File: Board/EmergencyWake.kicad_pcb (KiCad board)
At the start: 2 copper layers, 100 x 67 mm, 146 parts, among them J1 USB_C_Receptacle_USB2.0, J10 Conn_01x04, J2 Micro_SD_Card_Det, J3 Conn_01x03, J4 Conn_01x02, J5 Conn_01x05, J6 Conn_01x04, J7 Conn_01x02, J8 Conn_01x04, J9 Conn_01x04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

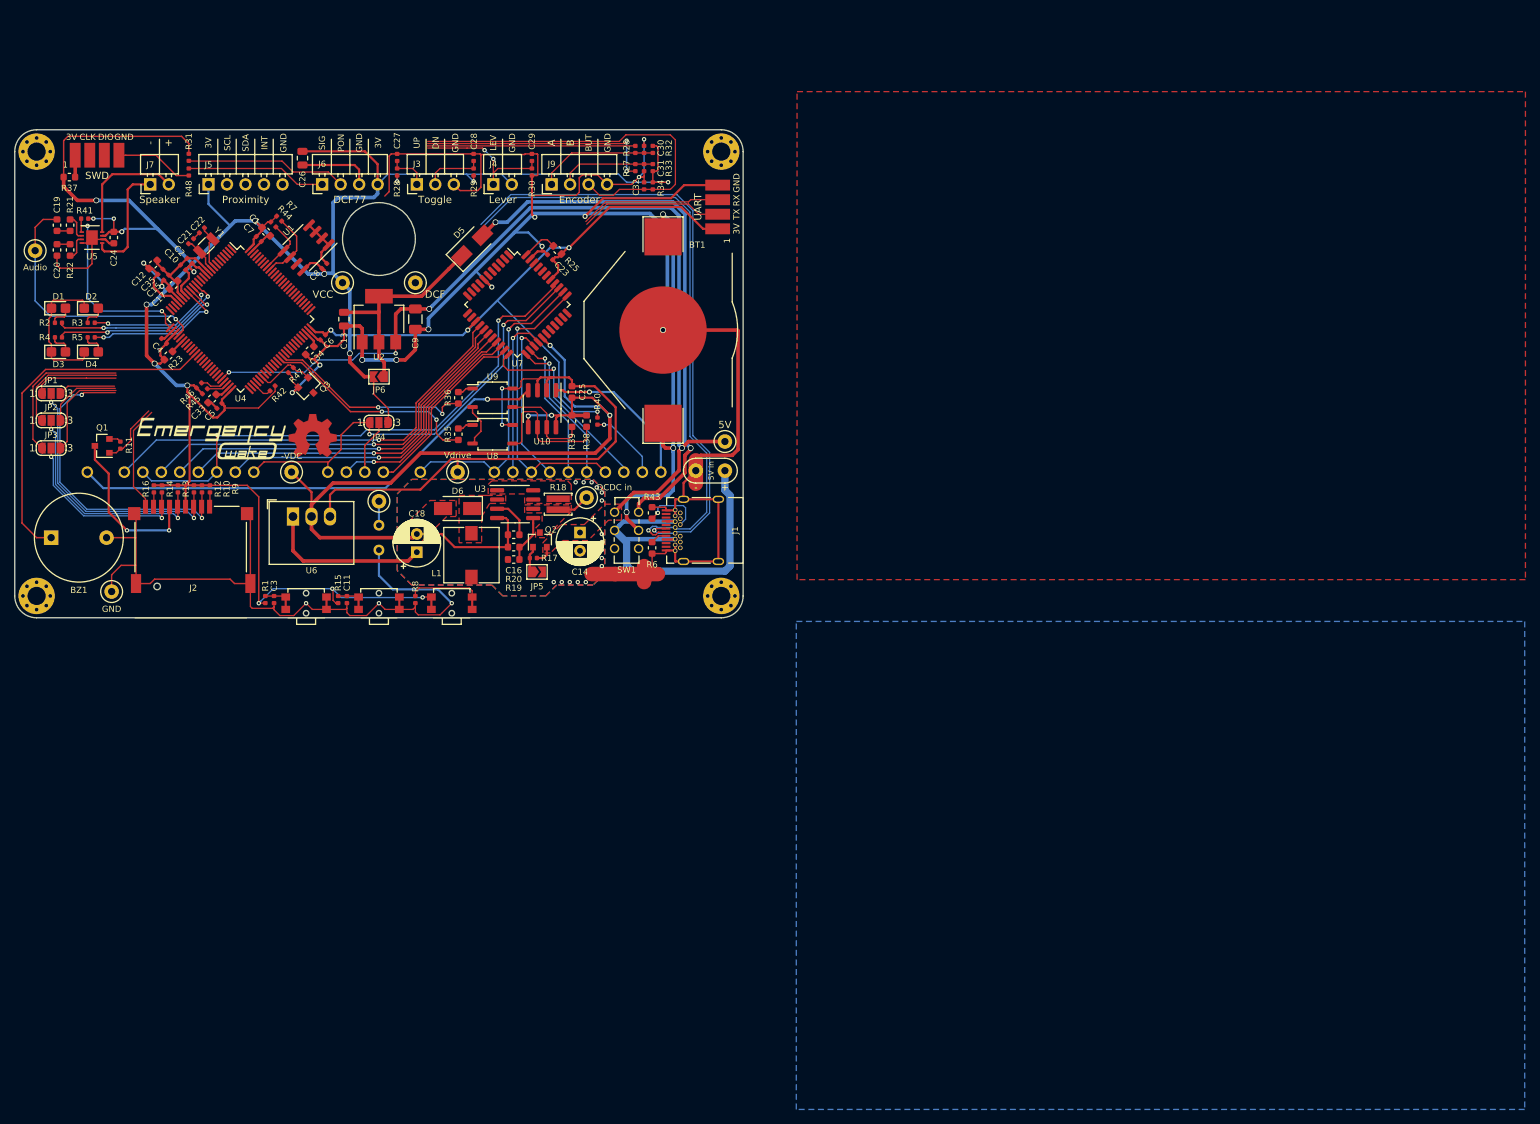
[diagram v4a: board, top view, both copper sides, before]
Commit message: [Board] More routing
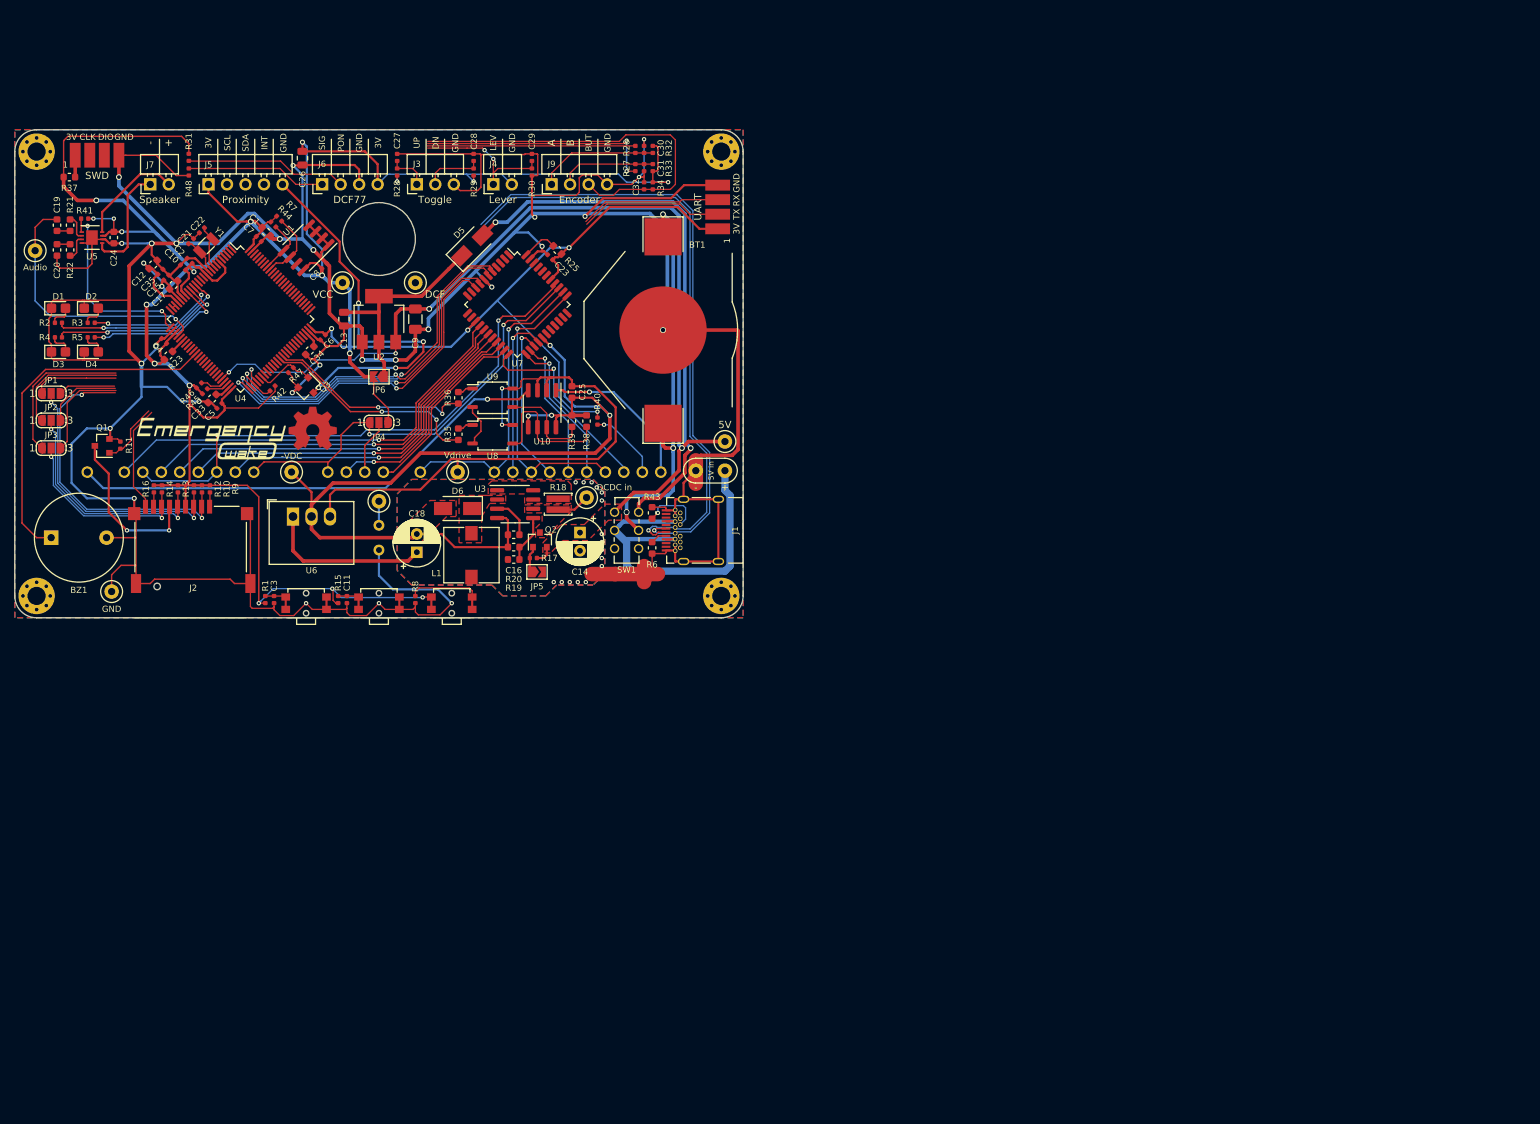
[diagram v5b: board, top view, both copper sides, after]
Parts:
- moved REF** 1.00 mm to (140.9, 141.0)
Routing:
- net GND: track 476.7 -> 629.2 mm, vias 15 -> 27
- net Net-(J5-Pad5): track 0.00 -> 53.1 mm, vias 0 -> 4
- net /VFD_DOUT: track 2.83 -> 52.5 mm, vias 0 -> 2
- net /VFD_DIN: track 0.00 -> 49.6 mm, vias 0 -> 2
- net /VFD_STB: track 0.00 -> 47.5 mm, vias 0 -> 2
- net /VFD_CLK: track 0.00 -> 47.5 mm, vias 0 -> 2
- net VCC: track 469.1 -> 480.1 mm, vias 23 -> 24
- net /SP-: track 16.8 -> 14.6 mm
- net +5V: track 131.6 -> 132.5 mm
- net /LEVER: track 19.7 -> 20.2 mm

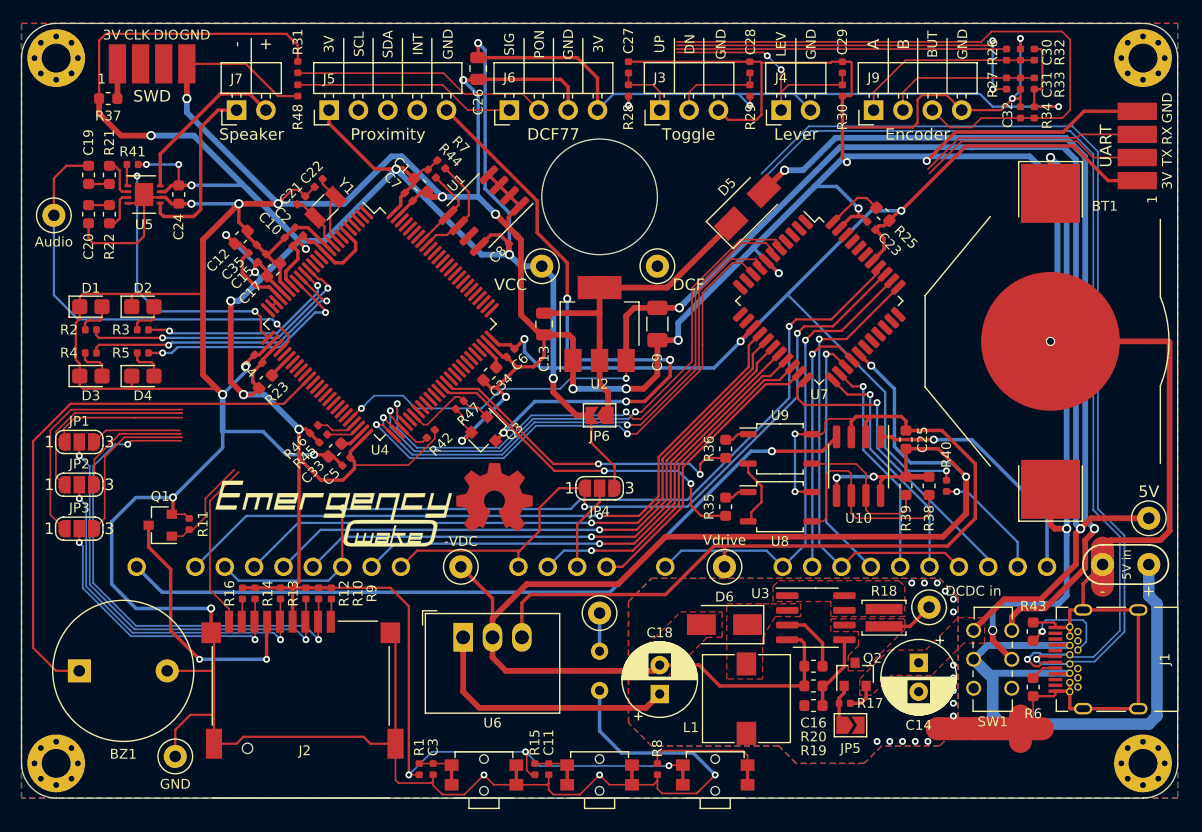
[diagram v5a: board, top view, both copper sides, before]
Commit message: [Board] Routed USB, UART and buttons
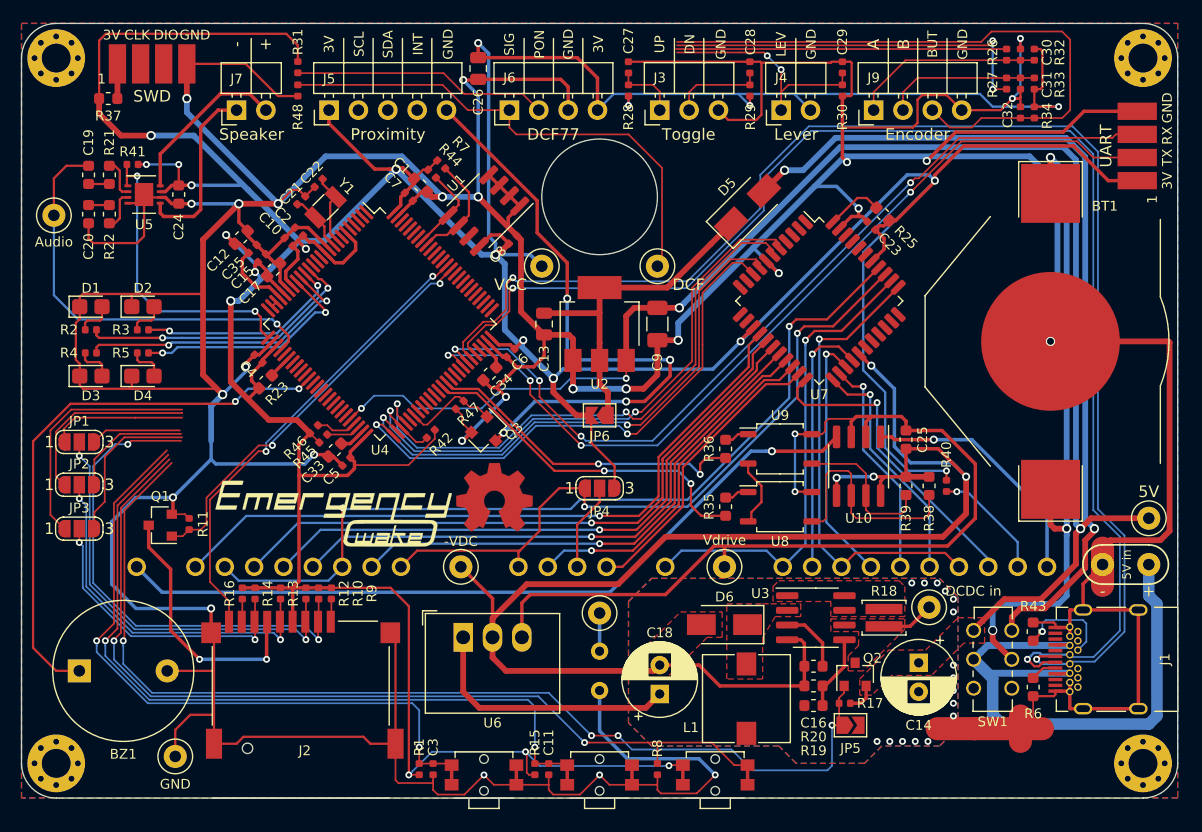
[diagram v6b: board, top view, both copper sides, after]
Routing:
- net /DCDC_EN: track 3.69 -> 92.5 mm, vias 0 -> 4
- net /BOOT0: track 11.3 -> 81.4 mm, vias 0 -> 2
- net /USR_BUT: track 4.56 -> 68.1 mm, vias 0 -> 2
- net /UART_TX: track 19.7 -> 76.8 mm, vias 0 -> 4
- net /UART_RX: track 19.3 -> 75.6 mm, vias 0 -> 4
- net /RESET: track 4.56 -> 59.1 mm, vias 0 -> 2
- net /USB_DM: track 84.8 -> 121.6 mm, vias 1 -> 2
- net /USB_DP: track 85.3 -> 120.7 mm, vias 1 -> 2
- net /SD_EN: track 8.72 -> 35.4 mm, vias 0 -> 2
- net /SD_DET: track 14.7 -> 40.6 mm, vias 0 -> 2
- net /DCF_SIG: track 19.2 -> 44.0 mm
- net VCC: track 480.1 -> 493.1 mm, vias 24 -> 22
- net /BUZZER: vias 0 -> 2

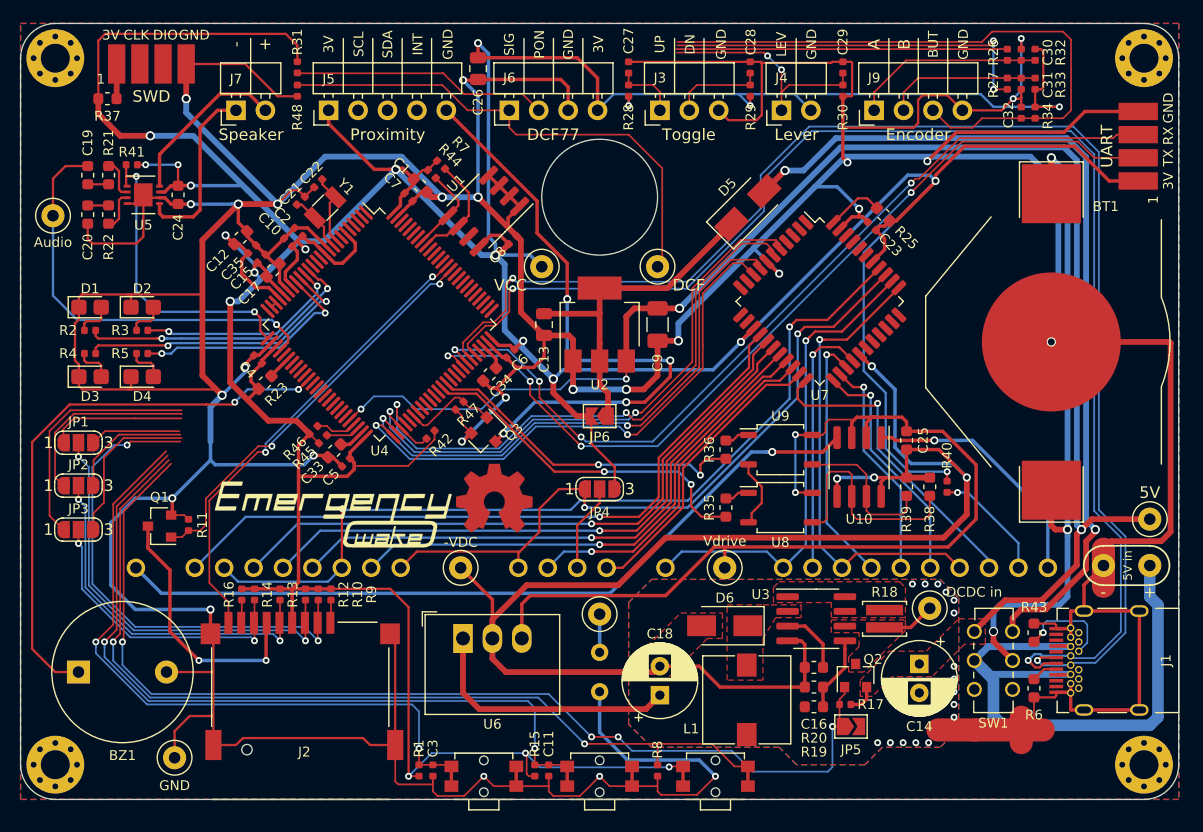
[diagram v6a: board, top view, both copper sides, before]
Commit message: [Board] Added TVS diodes for USB
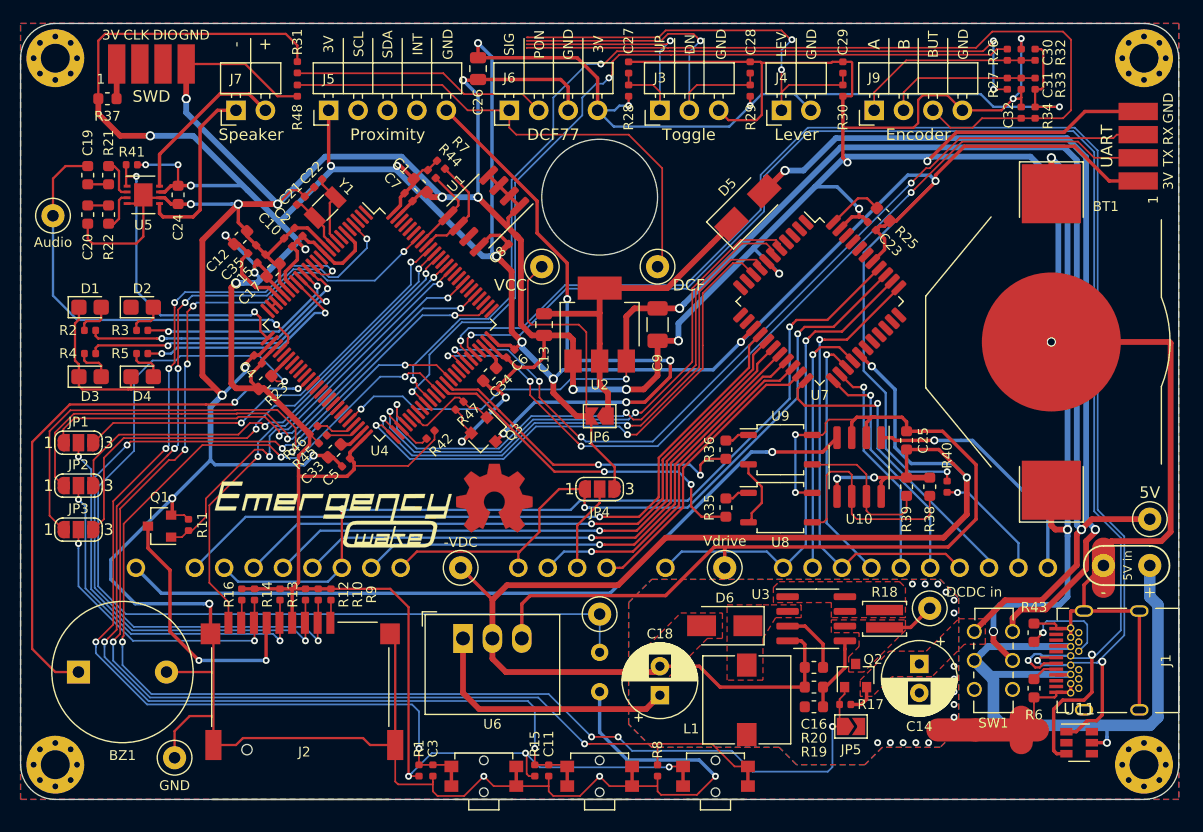
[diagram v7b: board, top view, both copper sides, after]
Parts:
- added U11: SRV05-4, Package_TO_SOT_SMD:SOT-23-6, F.Cu at (191.4, 162.1)
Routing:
- net Net-(R23-Pad2): track 5.39 -> 84.9 mm, vias 0 -> 1
- net /ENC_B: track 32.9 -> 78.6 mm, vias 2 -> 4
- net /ENC_A: track 28.6 -> 73.7 mm, vias 0 -> 2
- net /BOOT0: track 81.4 -> 118.3 mm, vias 2 -> 6
- net /USR_BUT: track 68.1 -> 102.6 mm, vias 2 -> 6
- net /SD_CK: track 16.5 -> 48.2 mm, vias 0 -> 2
- net /SD_CS: track 43.8 -> 74.9 mm, vias 2 -> 4
- net /SD_CMD: track 11.8 -> 42.6 mm, vias 0 -> 2
- net /RESET: track 59.1 -> 89.5 mm, vias 2 -> 6
- net /SD_D0: track 21.1 -> 51.1 mm, vias 0 -> 2
- net /SD_SCK: track 10.6 -> 40.0 mm, vias 0 -> 2
- net /SD_MISO: track 14.0 -> 43.3 mm, vias 0 -> 2
- net /SD_MOSI: track 7.81 -> 37.1 mm, vias 0 -> 2
- net /DCDC_EN: track 92.5 -> 119.7 mm, vias 4 -> 6
- net /TOGGLE_DOWN: track 8.10 -> 30.0 mm, vias 0 -> 1
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
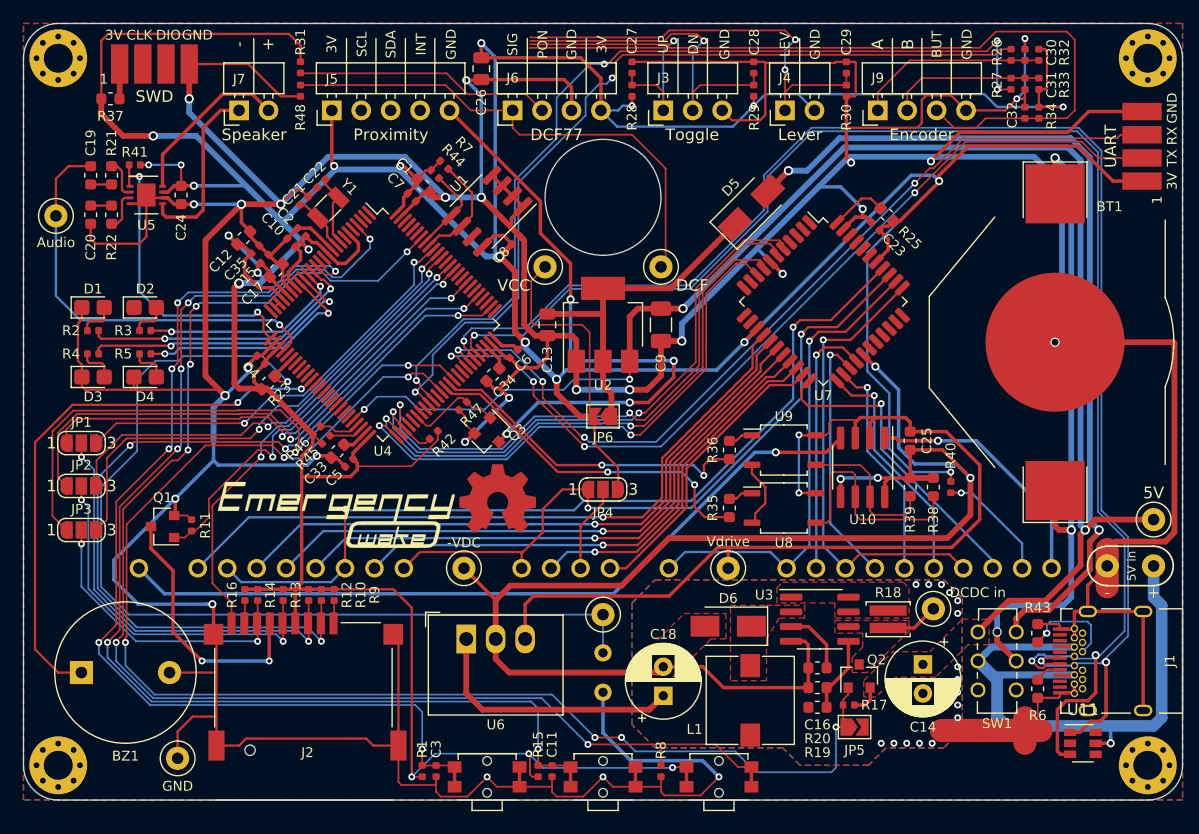
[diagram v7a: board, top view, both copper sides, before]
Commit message: [Board] Routing done, cleanup necessary
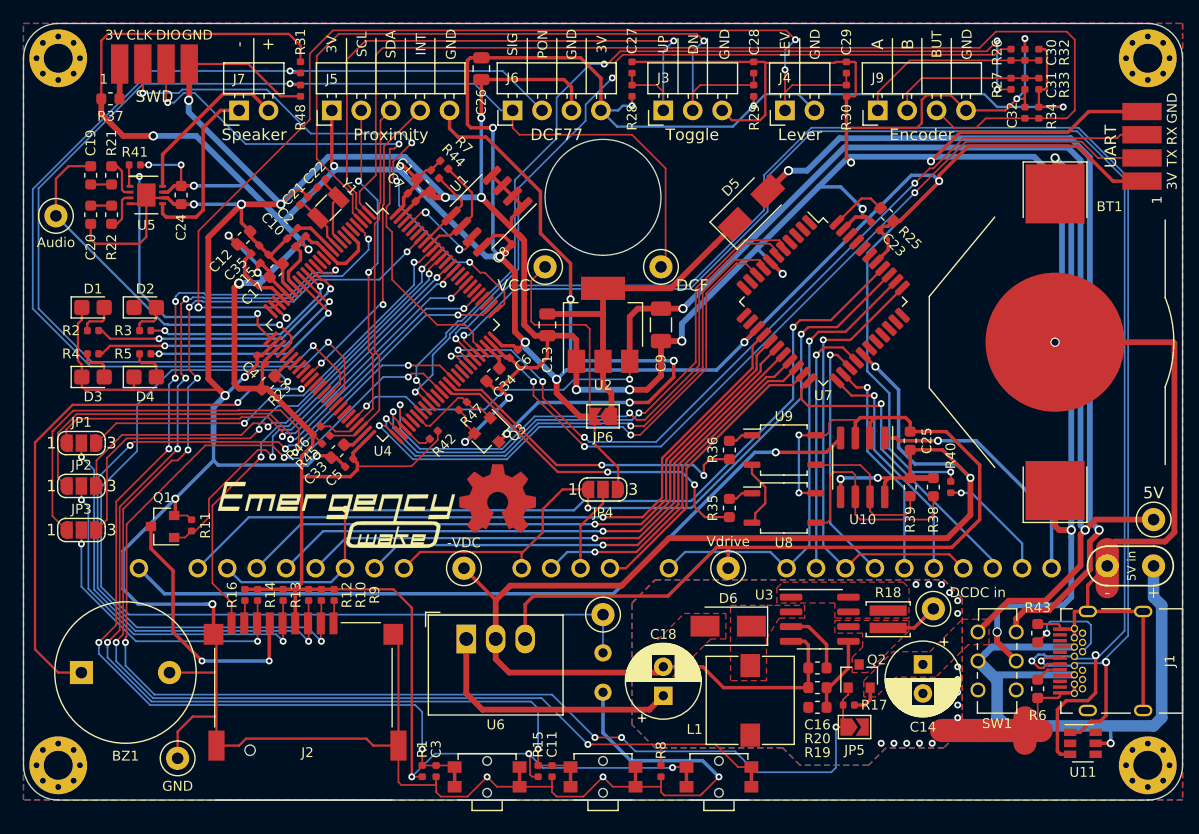
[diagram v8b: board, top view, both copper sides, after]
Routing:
- net /DCF_PON: track 22.2 -> 95.3 mm, vias 0 -> 2
- net /DCF_SIG: track 44.0 -> 113.6 mm, vias 0 -> 2
- net /LEVER: track 37.0 -> 91.9 mm, vias 2 -> 4
- net /SWDIO: track 0.00 -> 48.9 mm, vias 0 -> 2
- net /SWCLK: track 0.00 -> 48.3 mm, vias 0 -> 4
- net /TOGGLE_DOWN: track 30.0 -> 64.7 mm
- net /TOGGLE_UP: track 24.5 -> 55.0 mm
- net /I2C_SCL: track 3.54 -> 32.5 mm, vias 0 -> 2
- net /I2C_SDA: track 2.91 -> 31.8 mm
- net /ENC_BUT: track 67.1 -> 95.2 mm
- net /I2C_INT: track 0.00 -> 27.1 mm, vias 0 -> 2
- net /EEPROM_NWC: track 0.00 -> 8.15 mm, vias 0 -> 2
- net /AUDIO_OUT: track 36.8 -> 32.8 mm
- net GND: track 607.7 -> 605.2 mm
- net Net-(R23-Pad2): track 84.9 -> 82.7 mm
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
